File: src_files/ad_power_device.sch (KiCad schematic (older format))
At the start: 0 parts

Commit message: wifi module complete
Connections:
- no-connect marks 0 -> 1
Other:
- note added: "WIFI/BT MODULE"

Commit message: sata updated
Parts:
- added J?: 5622-6309-ML, greencharge-footprints:3M_5622-6309-ML, symbol 5622-6309-ML:5622-6309-ML
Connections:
- new net +12V: J?.P13 (V12_P13), J?.P14 (V12_P14), J?.P15 (V12_P15)
- new net +3V3: J?.P1 (V33_P1), J?.P2 (V33_P2), J?.P3 (V33_P3)
- new net +5V: J?.P7 (V5_P7), J?.P8 (V5_P8), J?.P9 (V5_P9)
- new net GND: J?.P10 (GND_P10), J?.P12 (GND_P12), J?.P4 (GND_P4), J?.P5 (GND_P5), J?.P6 (GND_P6), J?.S1 (GND_S1), J?.S4 (GND_S4), J?.S7 (GND_S7)
- new net SATA1_RX+: J?.S5 (B-), J?.S6 (B+)
- new net SATA1_TX+: J?.S2 (A+)
- new net SATA1_TX-: J?.S3 (A-)
- no-connect marks 1 -> 2
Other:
- note added: "LINKS OF REF:\nhttps://www.tonymacx86.com/media/sata-power-pinout.63971/\nhttps://pinoutguide.com/Power/sata-power_pinout.shtml"
- note added: "SATA/HDD CONN"
- note added: "z0=90Ohm"

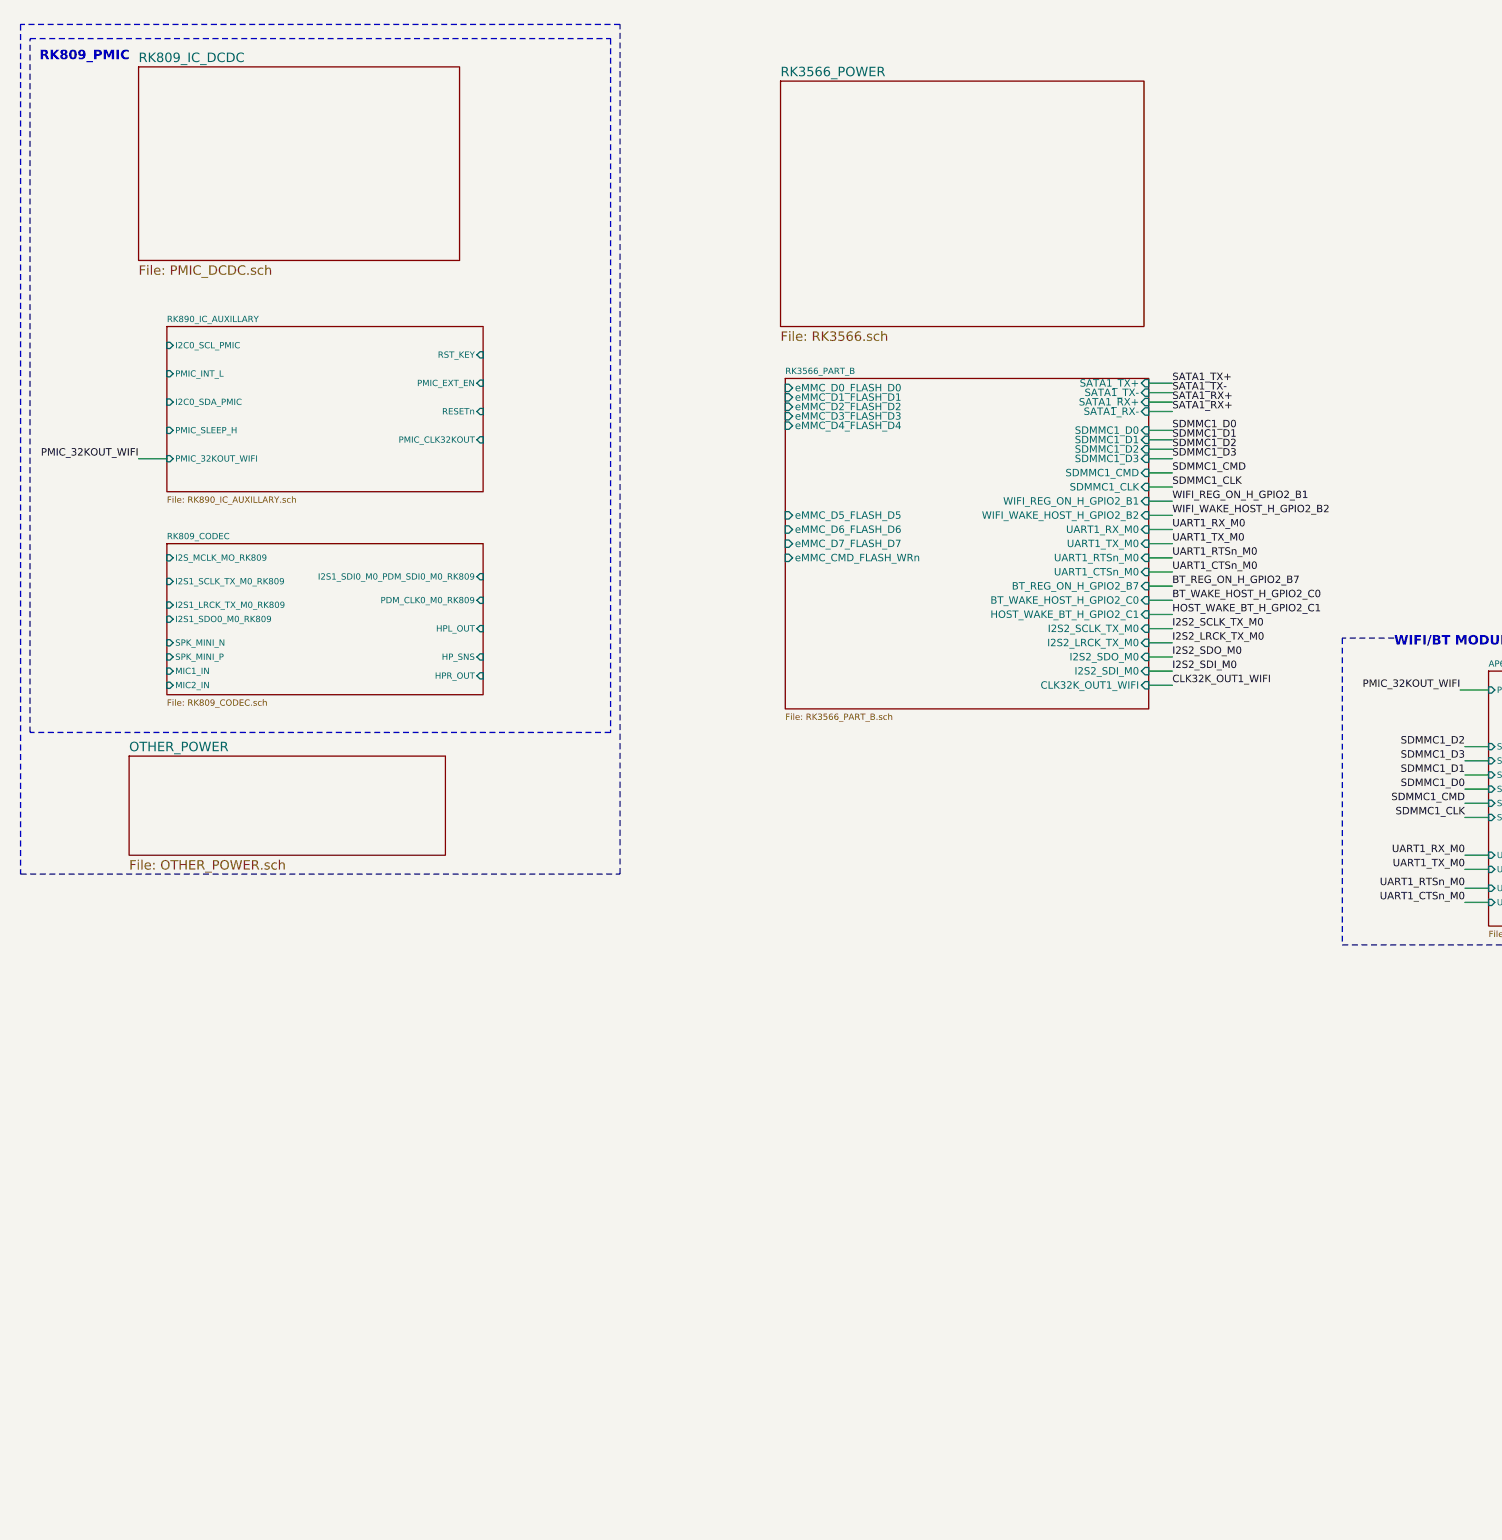
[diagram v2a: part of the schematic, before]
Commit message: LPDDR3 SECTION COMPLETE
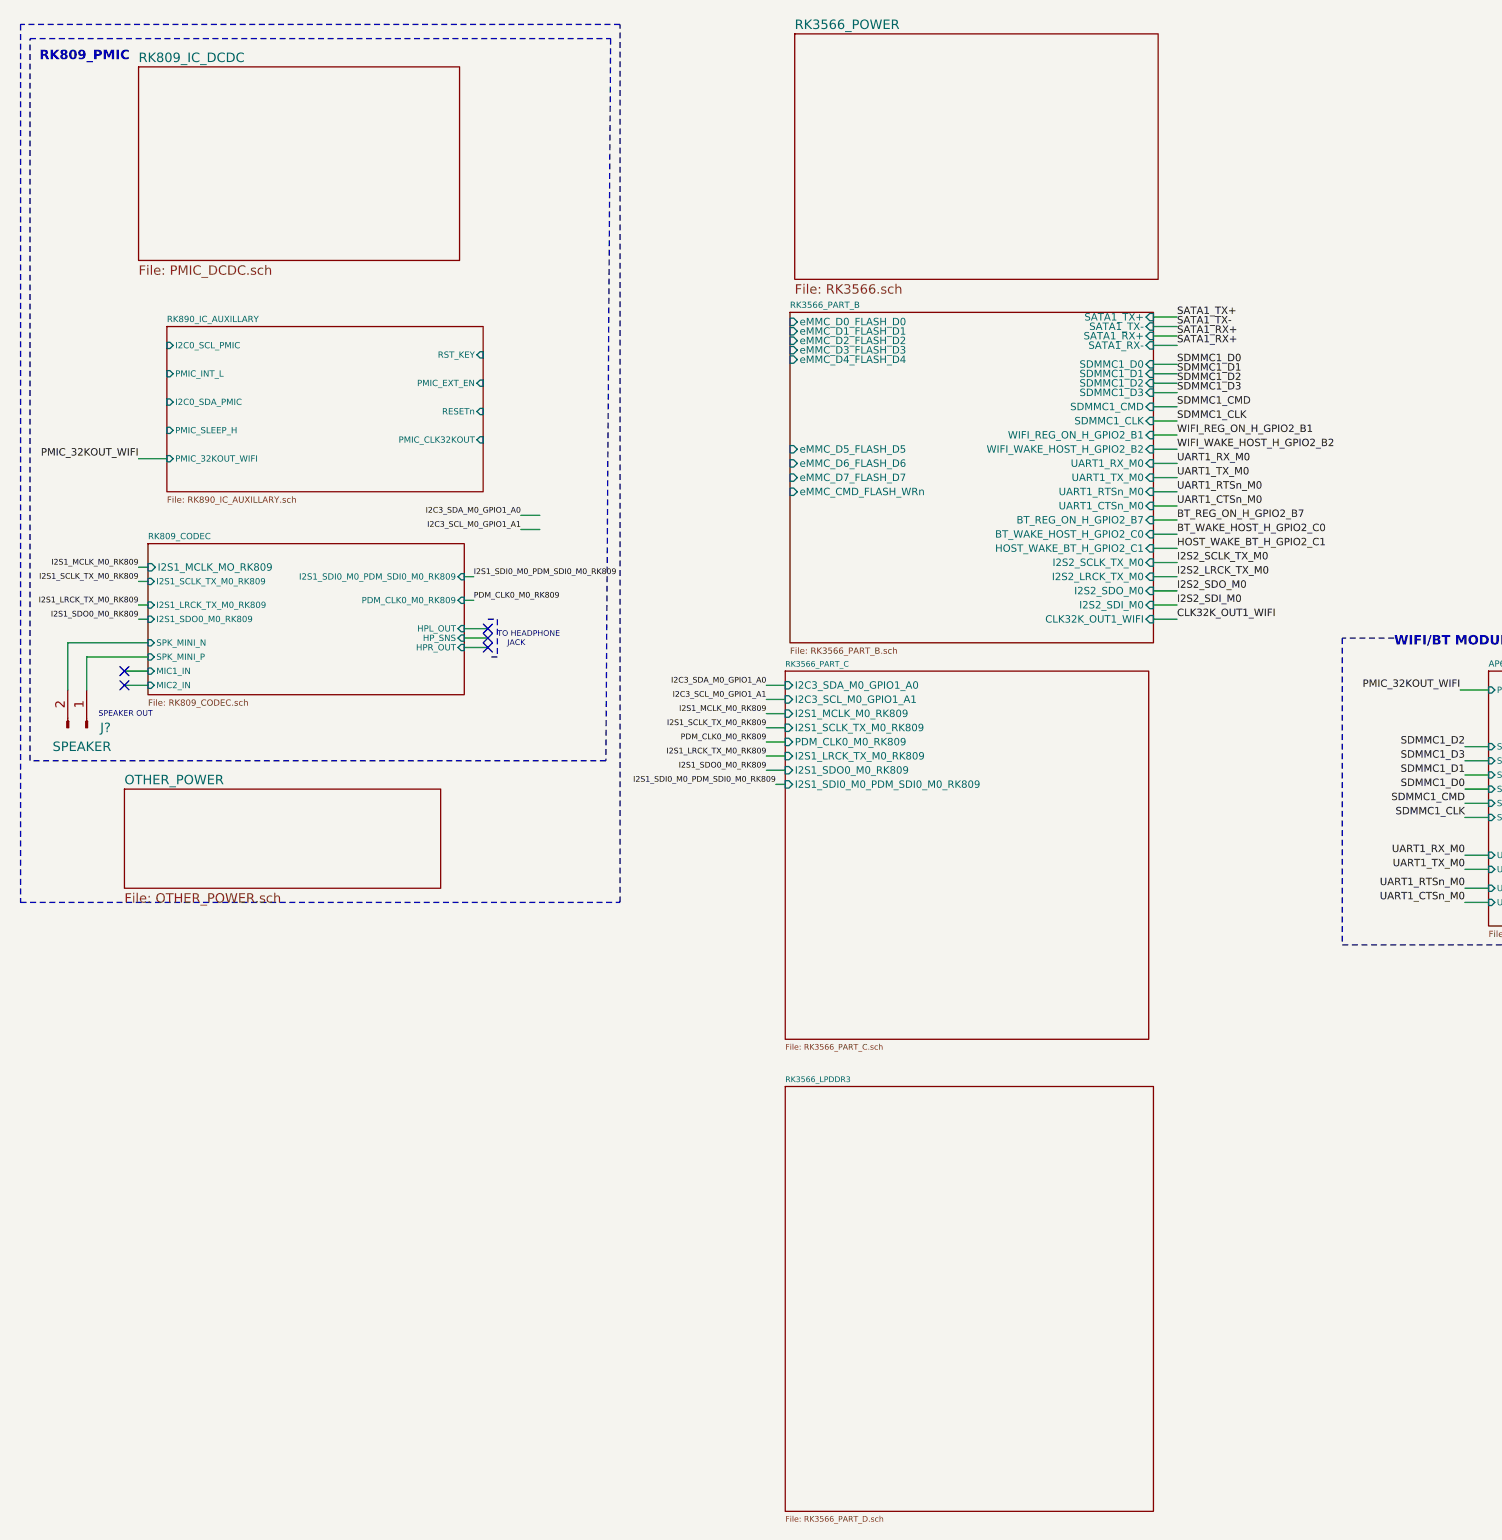
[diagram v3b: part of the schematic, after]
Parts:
- added J?: SPEAKER, symbol Connector:Conn_01x02_Male
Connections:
- net RK809_CODEC/SPK_MINI_N: now also J?.2 (Pin_2)
- net RK809_CODEC/SPK_MINI_P: now also J?.1 (Pin_1)
- no-connect marks 2 -> 7
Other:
- note added: "SPEAKER OUT\n"
- note added: "TO HEADPHONE \n JACK"

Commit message: littleupdate
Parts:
- J1: renamed from J?; footprint (none) -> Connector_JST:JST_EH_B2B-EH-A_1x02_P2.50mm_Vertical
- gave numbers to parts that had none: 1
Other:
- moved on the sheet: J1, J2

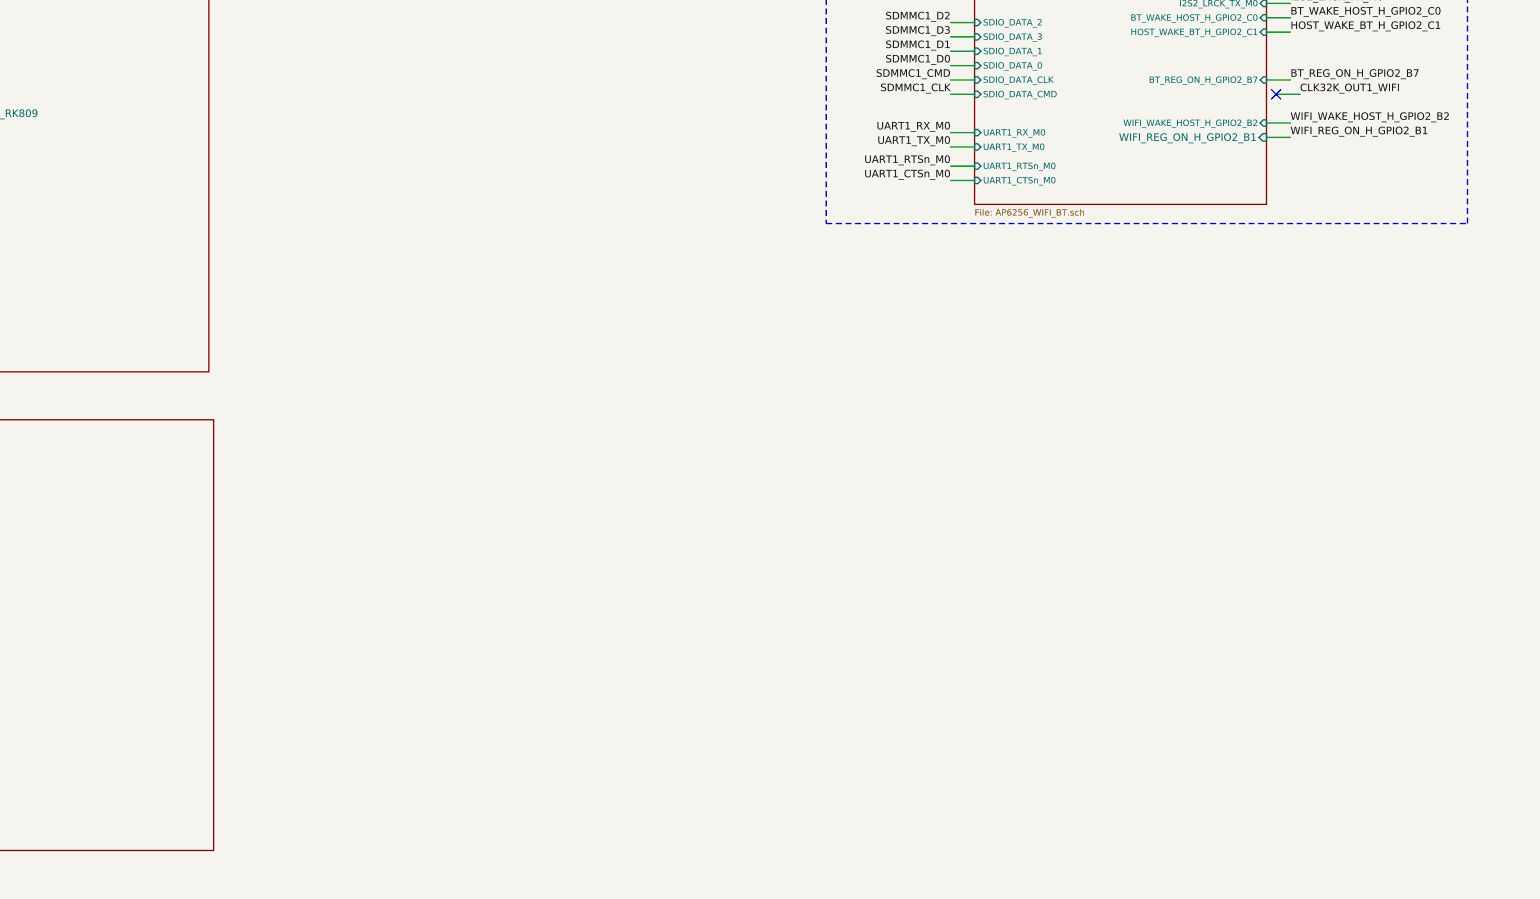
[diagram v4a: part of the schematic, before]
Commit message: gps add
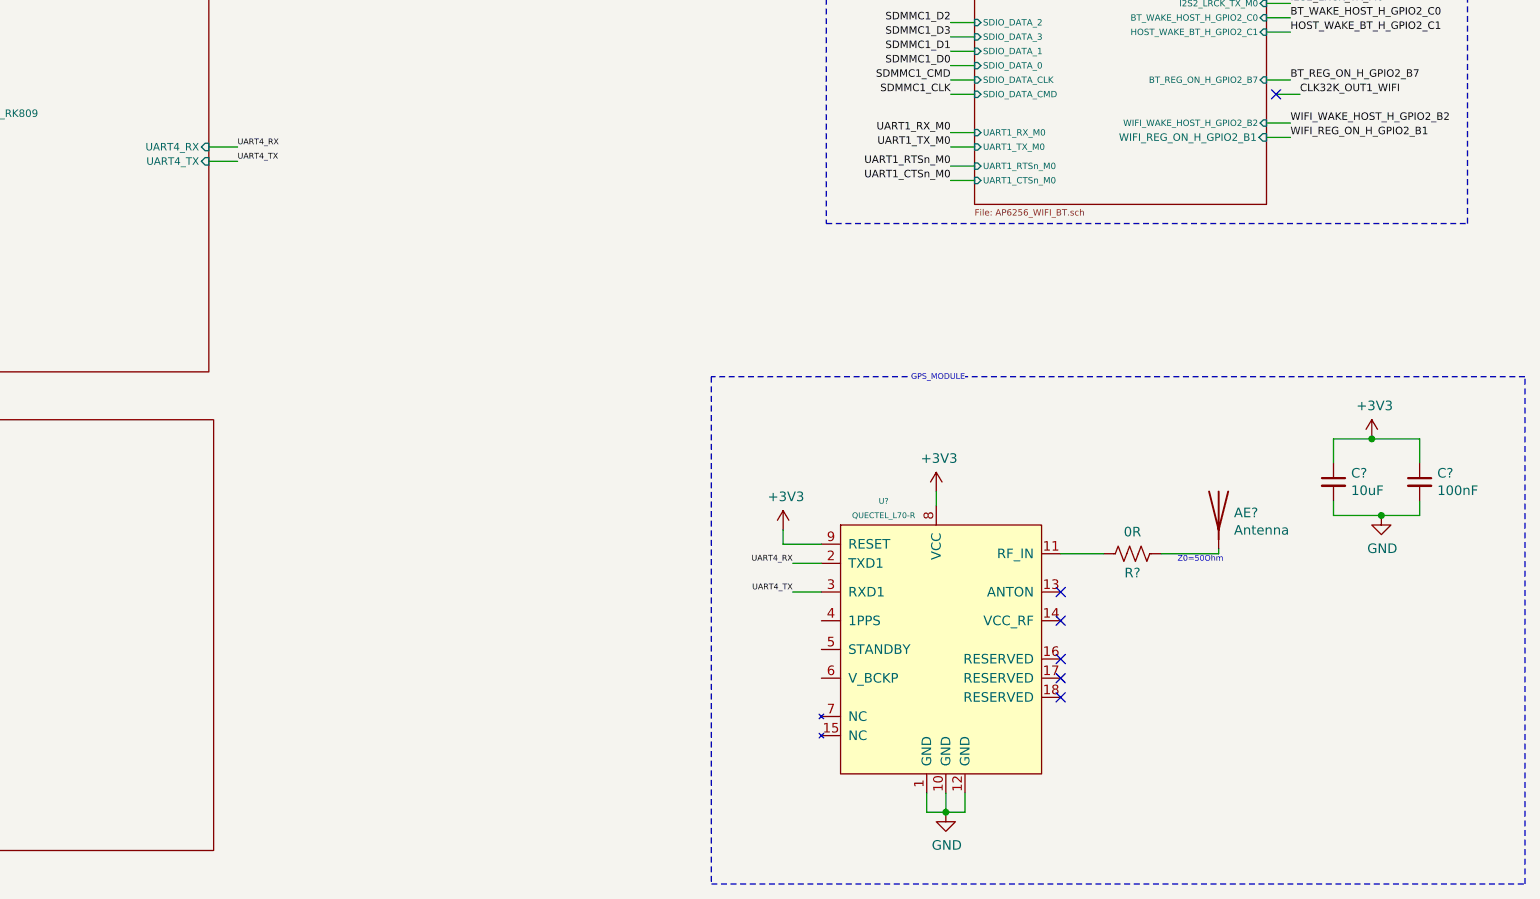
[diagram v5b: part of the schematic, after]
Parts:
- added AE?: Antenna, symbol Device:Antenna
- added C?: 10uF, symbol Device:C_Small
- added C?: 100nF, symbol Device:C_Small
- added R?: 0R, symbol Device:R_US
- added U?: QUECTEL_L70-R, greencharge-footprints:QUECTEL_L70-R, symbol GCL_Integrated-Circuits:QUECTEL_L70-R
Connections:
- net +3V3: now also C?.1, C?.1, U?.8 (VCC), U?.9 (RESET)
- net GND: now also C?.2, C?.2, U?.1 (GND), U?.10 (GND), U?.12 (GND)
- new net: R?.2, U?.11 (RF_IN)
- new net: AE?.1 (A), R?.1
- new net UART4_RX: U?.2 (TXD1)
- new net UART4_TX: U?.3 (RXD1)
- no-connect marks 7 -> 12
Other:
- note added: "GPS_MODULE"
- note added: "Z0=50Ohm\n"
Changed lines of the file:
@@
 F8 "I2S1_SDO0_M0_RK809" I L 7150 4800 39
 F9 "I2S1_SDI0_M0_PDM_SDI0_M0_RK809" I L 7150 4875 39
+F10 "UART4_RX" I R 9075 5050 39
+F11 "UART4_TX" I R 9075 5125 39
 $EndSheet
 Wire Wire Line
@@
 Wire Notes Line
 	2650 675  4575 675
+$Comp
+L OLIMEX_Power:GND #PWR?
+U 1 1 63970D52
+P 12925 8525
+F 0 "#PWR?" H 12925 8275 50  0001 C CNN
+F 1 "GND" H 12930 8352 50  0000 C CNN
+F 2 "" H 12925 8525 60  0000 C CNN
+F 3 "" H 12925 8525 60  0000 C CNN
+	1    12925 8525
+	1    0    0    -1
+$EndComp
+Connection ~ 12925 8525
+Wire Wire Line
+	12925 8525 13025 8525
+$Comp
+L Device:C_Small C?
+U 1 1 6398AD67
+P 14950 6800
+F 0 "C?" H 15042 6846 50  0000 L CNN
+F 1 "10uF" H 15042 6755 50  0000 L CNN
+F 2 "" H 14950 6800 50  0001 C CNN
+F 3 "~" H 14950 6800 50  0001 C CNN
+	1    14950 6800
+	1    0    0    -1
+$EndComp
+$Comp
+L power:+3V3 #PWR?
+U 1 1 6398B1BF
+P 15150 6575
+F 0 "#PWR?" H 15150 6425 50  0001 C CNN
+F 1 "+3V3" H 15165 6748 50  0000 C CNN
+F 2 "" H 15150 6575 50  0001 C CNN
+F 3 "" H 15150 6575 50  0001 C CNN
+	1    15150 6575
+	1    0    0    -1
+$EndComp
+$Comp
+L Device:C_Small C?
+U 1 1 6398B8E7
+P 15400 6800
+F 0 "C?" H 15492 6846 50  0000 L CNN
+F 1 "100nF" H 15492 6755 50  0000 L CNN
+F 2 "" H 15400 6800 50  0001 C CNN
+F 3 "~" H 15400 6800 50  0001 C CNN
+	1    15400 6800
+	1    0    0    -1
+$EndComp
+$Comp
+L OLIMEX_Power:GND #PWR?
+U 1 1 63991D90
+P 15200 6975
+F 0 "#PWR?" H 15200 6725 50  0001 C CNN
+F 1 "GND" H 15205 6802 50  0000 C CNN
+F 2 "" H 15200 6975 60  0000 C CNN
+F 3 "" H 15200 6975 60  0000 C CNN
+	1    15200 6975
+	1    0    0    -1
+$EndComp
+Wire Wire Line
+	15150 6575 14950 6575
+Wire Wire Line
+	14950 6575 14950 6700
+Wire Wire Line
+	14950 6975 15200 6975
+Wire Wire Line
+	15400 6975 15400 6900
+Wire Wire Line
+	14950 6900 14950 6975
+Wire Wire Line
+	15400 6700 15400 6575
+Wire Wire Line
+	15400 6575 15150 6575
+Connection ~ 15150 6575
+Connection ~ 15200 6975
+Wire Wire Line
+	15200 6975 15400 6975
+$Comp
+L power:+3V3 #PWR?
+U 1 1 639B3FF1
+P 12875 6850
+F 0 "#PWR?" H 12875 6700 50  0001 C CNN
+F 1 "+3V3" H 12890 7023 50  0000 C CNN
+F 2 "" H 12875 6850 50  0001 C CNN
+F 3 "" H 12875 6850 50  0001 C CNN
+	1    12875 6850
+	1    0    0    -1
+$EndComp
+Text Label 9225 5050 0    30   ~ 0
+UART4_RX
+Text Label 9225 5125 0    30   ~ 0
+UART4_TX
+Wire Wire Line
+	9075 5050 9225 5050
+Wire Wire Line
+	9075 5125 9225 5125
+Wire Notes Line
+	15950 8900 15950 6250
+Wire Notes Line
+	15950 6250 13025 6250
+Wire Wire Line
+	12875 6925 12875 6850
+NoConn ~ 13525 7925
+NoConn ~ 13525 7825
+NoConn ~ 13525 7725
+Wire Wire Line
+	13025 8525 13025 8425
+Wire Wire Line
+	12925 8425 12925 8525
+Wire Notes Line
+	11700 8900 15950 8900
+Wire Notes Line
+	11700 6250 11700 8900
+Wire Notes Line
+	12725 6250 11700 6250
+Text Notes 13025 6275 2    30   ~ 0
+GPS_MODULE
+Wire Wire Line
+	12075 7125 12075 7050
+Wire Wire Line
+	12275 7125 12075 7125
+$Comp
+L power:+3V3 #PWR?
+U 1 1 63A0309F
+P 12075 7050
+F 0 "#PWR?" H 12075 6900 50  0001 C CNN
+F 1 "+3V3" H 12090 7223 50  0000 C CNN
+F 2 "" H 12075 7050 50  0001 C CNN
+F 3 "" H 12075 7050 50  0001 C CNN
+	1    12075 7050
+	1    0    0    -1
+$EndComp
+Wire Wire Line
+	12275 7375 12125 7375
+Wire Wire Line
+	12275 7225 12125 7225
+Text Label 12125 7375 2    30   ~ 0
+UART4_TX
+Text Label 12125 7225 2    30   ~ 0
+UART4_RX
+Wire Wire Line
+	12825 8525 12925 8525
+Wire Wire Line
+	12825 8425 12825 8525
+$Comp
+L Device:Antenna AE?
+U 1 1 63A53DB1
+P 14350 6950
+F 0 "AE?" H 14430 6939 50  0000 L CNN
+F 1 "Antenna" H 14430 6848 50  0000 L CNN
+F 2 "" H 14350 6950 50  0001 C CNN
+F 3 "~" H 14350 6950 50  0001 C CNN
+	1    14350 6950
+	1    0    0    -1
+$EndComp
+$Comp
+L Device:R_US R?
+U 1 1 63A54505
+P 13900 7175
+F 0 "R?" V 14000 7175 50  0000 C CNN
+F 1 "0R" V 13786 7175 50  0000 C CNN
+F 2 "" V 13940 7165 50  0001 C CNN
+F 3 "~" H 13900 7175 50  0001 C CNN
+	1    13900 7175
+	0    1    1    0
+$EndComp
+Wire Wire Line
+	13525 7175 13750 7175
+Wire Wire Line
+	14350 7175 14350 7150
+Wire Wire Line
+	14050 7175 14350 7175
+Text Notes 14375 7225 2    30   ~ 0
+Z0=50Ohm\n
+$Comp
+L GCL_Integrated-Circuits:QUECTEL_L70-R U?
+U 1 1 6397091B
+P 12625 6875
+F 0 "U?" H 12600 6850 30  0000 C CNN
+F 1 "QUECTEL_L70-R" H 12600 6775 30  0000 C CNN
+F 2 "greencharge-footprints:QUECTEL_L70-R" H 12825 6875 30  0001 C CNN
+F 3 "" H 12825 6875 30  0001 C CNN
+	1    12625 6875
+	1    0    0    -1
+$EndComp
+NoConn ~ 13525 7375
+NoConn ~ 13525 7525
 $EndSCHEMATC

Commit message: added 3 screens
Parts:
- added D1, D2: LED, LED_SMD:LED_0402_1005Metric, symbol Device:LED
- added H1, H2, H3, H4: MountingHole, MountingHole:MountingHole_2.2mm_M2_Pad, symbol Mechanical:MountingHole
- added J5, J6: 3-1734592-0, greencharge-footprints:TE_3-1734592-0, symbol 3-1734592-0:3-1734592-0
- added Q1, Q2: DTC143ZEBTL, greencharge-footprints:SOTFL50P160X85-3N, symbol DTC143ZEBTL:DTC143ZEBTL
- added R29, R30: 1K, Resistor_SMD:R_0402_1005Metric, symbol Device:R_US
- U7: renamed from U?; value QUECTEL_L70-R -> QUECTEL_L70-RL
- gave numbers to parts that had none: 4
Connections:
- net +3V3: now also D1.2 (A), D2.2 (A)
- net GND: now also Q1.2, Q2.2
- net IPPS: now reaches U7.4 (1PPS)
- net IPPS: now also Q1.1
- net STANDBY: now reaches U7.5 (STANDBY)
- net STANDBY: now also Q2.1
- new net: D1.1 (K), R29.1
- new net: D2.1 (K), R30.1
- new net: Q1.3, R29.2
- new net: Q2.3, R30.2
- new net: J5.S1 (SHIELD), J5.S2 (SHIELD)
- new net: J6.S1 (SHIELD), J6.S2 (SHIELD)
- no-connect marks 12 -> 14
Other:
- note added: "LCD_MIPI_GPIO"
- note added: "MOUNTING HOLES"
- note added: "TO CODEC"
- note added: "TO DISPLAY_0(MIPI_TX0)"
